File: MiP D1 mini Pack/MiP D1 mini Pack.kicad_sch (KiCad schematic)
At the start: 4 parts, among them J1 MiP, J2 Debug, U1 WEMOS D1 mini

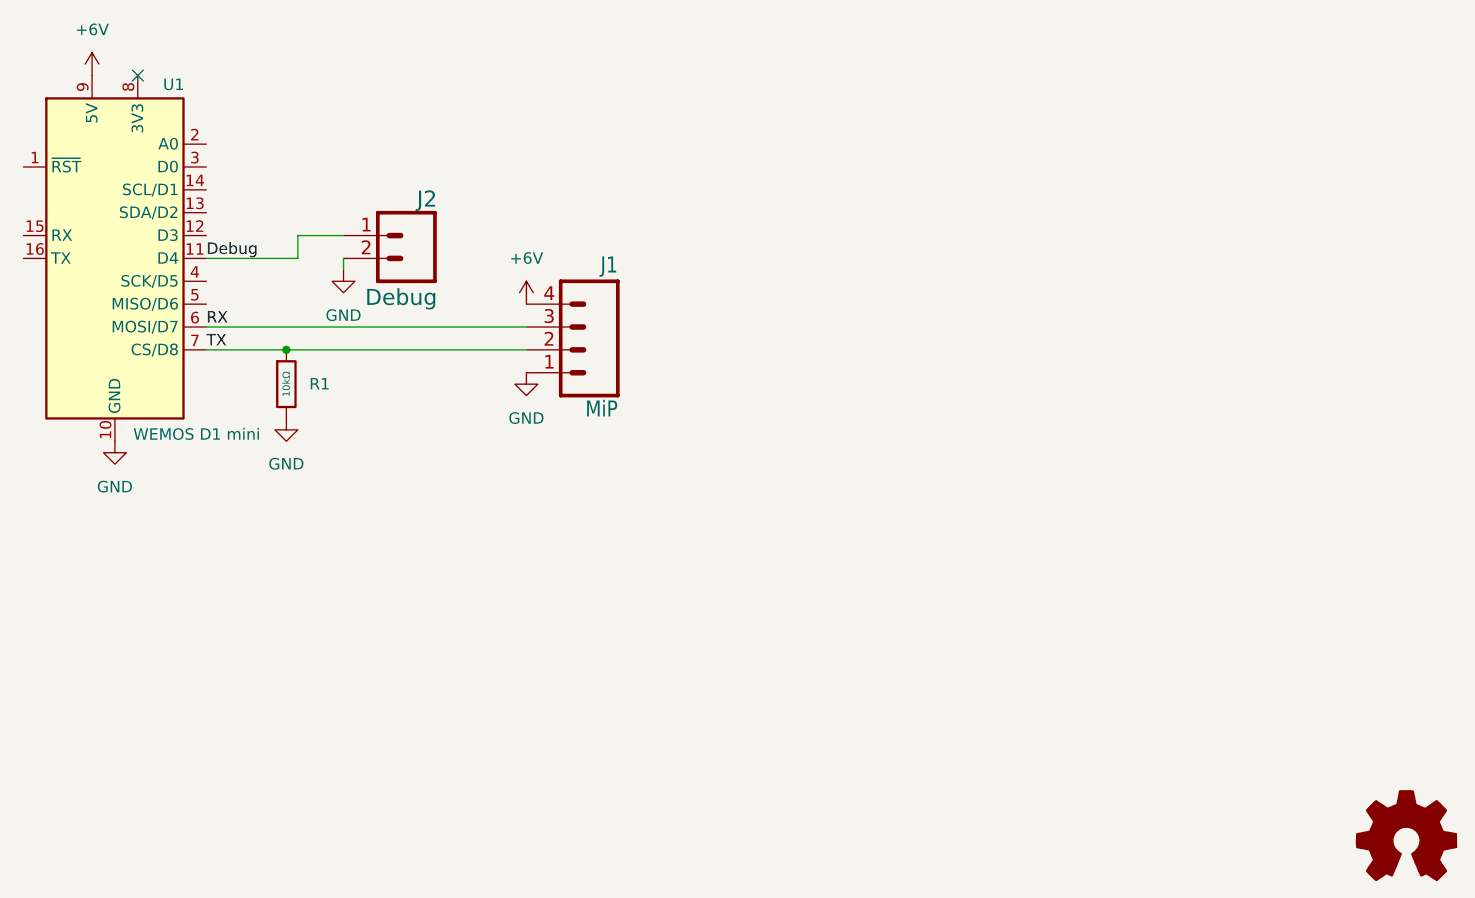
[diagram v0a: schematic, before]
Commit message: Using tri-state buffer
Using tri-state buffer, not resistor, to decouple D1 mini from MiP.
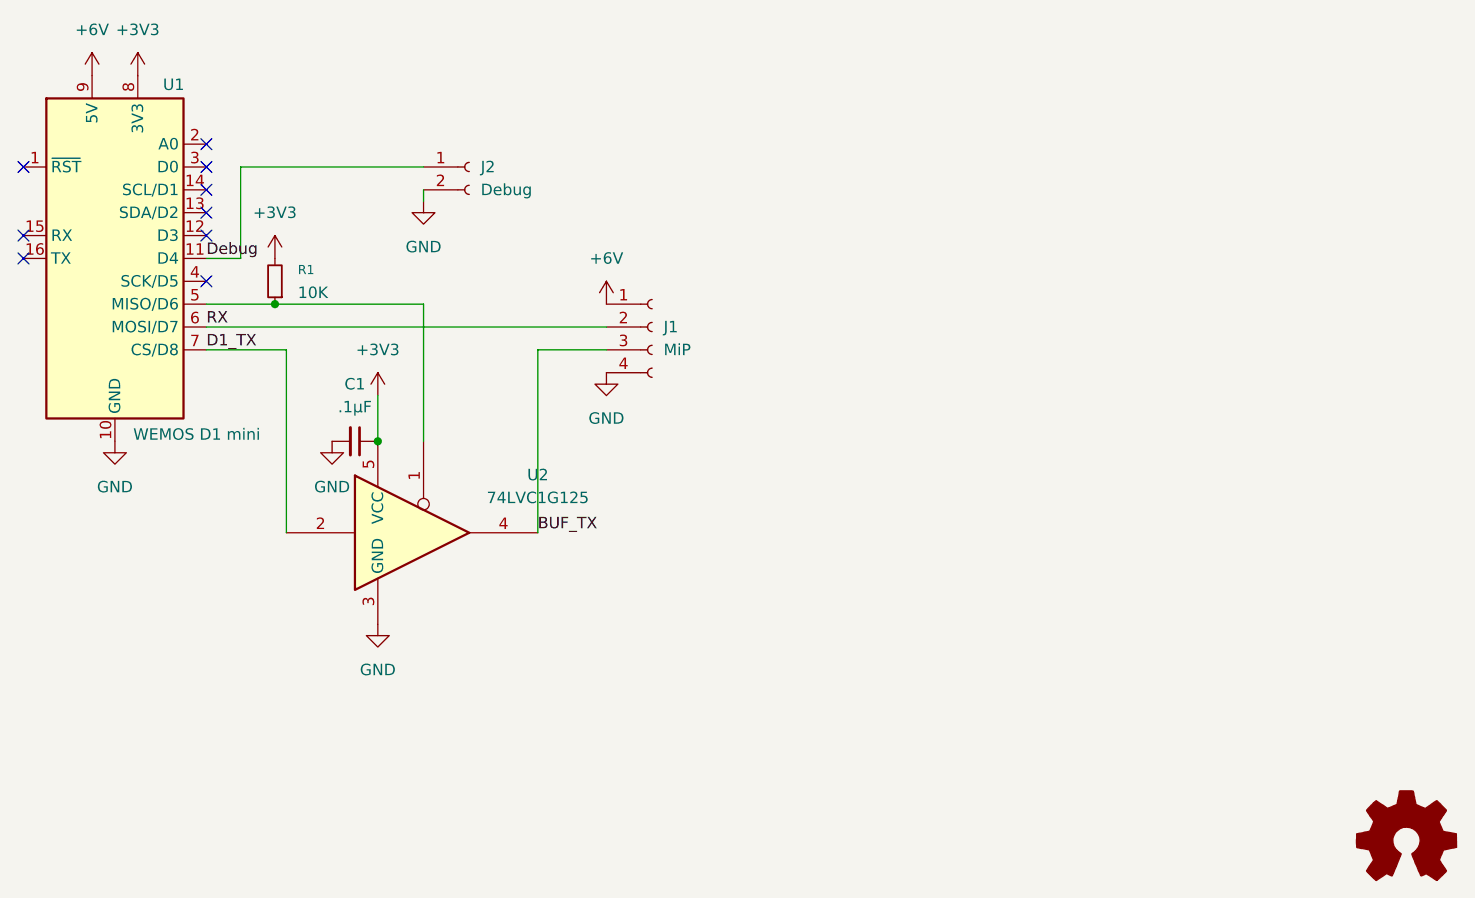
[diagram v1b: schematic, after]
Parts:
- removed J1: MiP, Connector_JST:JST_ZH_B4B-ZR_1x04_P1.50mm_Vertical, symbol MiP D1 mini Pack-eagle-import:M04JST
- removed J2: Debug, Connector_PinSocket_2.54mm:PinSocket_1x02_P2.54mm_Horizontal, symbol MiP D1 mini Pack-eagle-import:CONN_02PTH_RA_FEMALE
- removed R1: 10kΩ, Resistor_SMD:R_0805_2012Metric_Pad1.20x1.40mm_HandSolder, symbol PCM_JLCPCB-Resistors:0402,10kΩ
- added C1: .1μF, Capacitor_SMD:C_0805_2012Metric_Pad1.18x1.45mm_HandSolder, symbol Device:C_Small
- added J1: MiP, Connector_JST:JST_ZH_B4B-ZR_1x04_P1.50mm_Vertical, symbol Connector:Conn_01x04_Socket
- added J2: Debug, Connector_PinSocket_2.54mm:PinSocket_1x02_P2.54mm_Horizontal, symbol Connector:Conn_01x02_Socket
- added R1: 10K, Resistor_SMD:R_0805_2012Metric_Pad1.20x1.40mm_HandSolder, symbol Device:R_Small
- added U2: 74LVC1G125, Package_TO_SOT_SMD:SOT-23-5_HandSoldering, symbol 74xGxx:74LVC1G125
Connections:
- net +6V: now also J1.1 (Pin_1)
- net Debug: now also J2.1 (Pin_1)
- net GND: now also C1.2, J1.4 (Pin_4), J2.2 (Pin_2), U2.3 (GND)
- net RX: now also J1.2 (Pin_2)
- net D1_TX: now reaches U1.7 (CS/D8)
- net D1_TX: now also U2.2
- net at U1.5 (MISO/D6): now also R1.1, U2.1
- net +3V3: now reaches U1.8 (3V3)
- net +3V3: now also C1.1, R1.2, U2.5 (VCC)
- new net BUF_TX: J1.3 (Pin_3), U2.4
- no-connect marks 1 -> 9
